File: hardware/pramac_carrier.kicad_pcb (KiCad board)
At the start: 2 copper layers, 135 x 100 mm, 31 parts, among them J1 BATT+ / BATT-, J2 TAHO / CONTACT / GND, J3 Relay module VCC/IN1/IN2/GND, P1 LM2596 IN+/IN-, P2 LM2596 OUT+/OUT-, U1A ESP32 left, U1B ESP32 right, U3 LM393

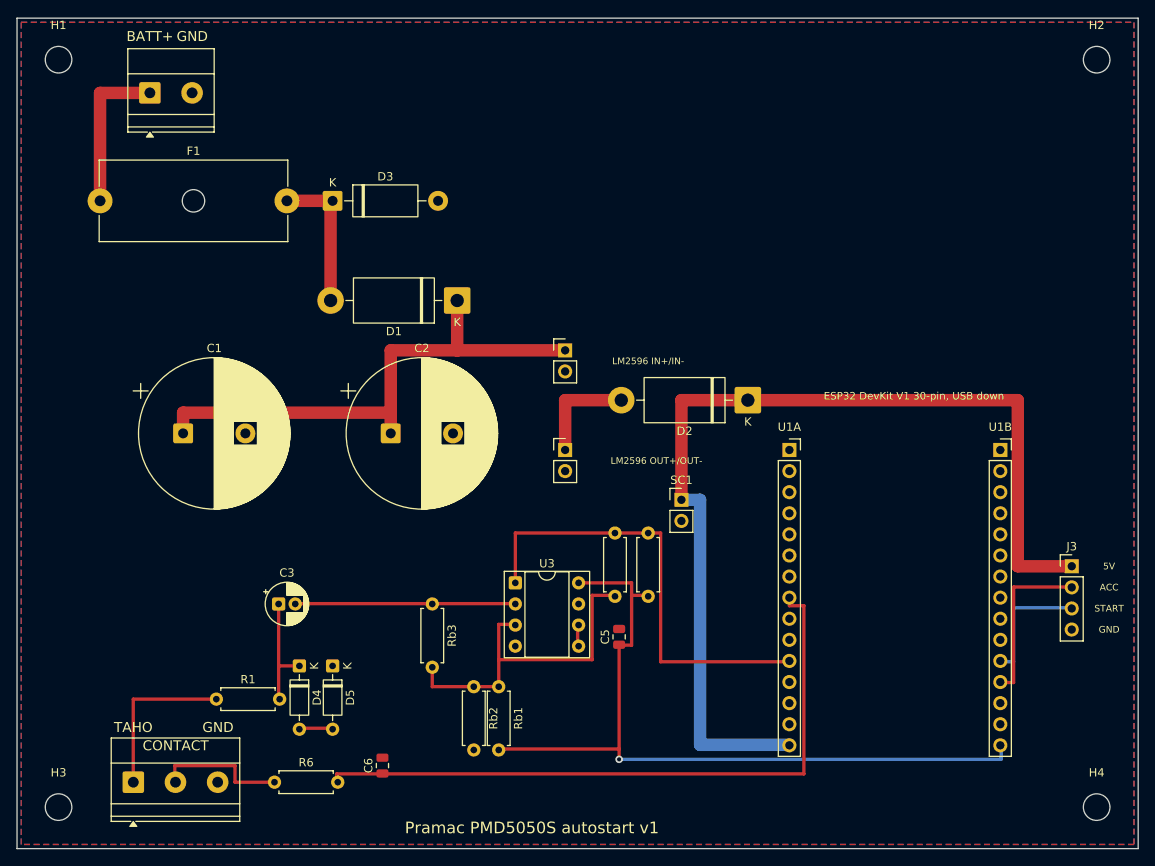
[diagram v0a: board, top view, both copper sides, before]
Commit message: Board v3: on-board relays with NPN drivers, RM20S DC-DC, charger input, one-side terminals, full BOM
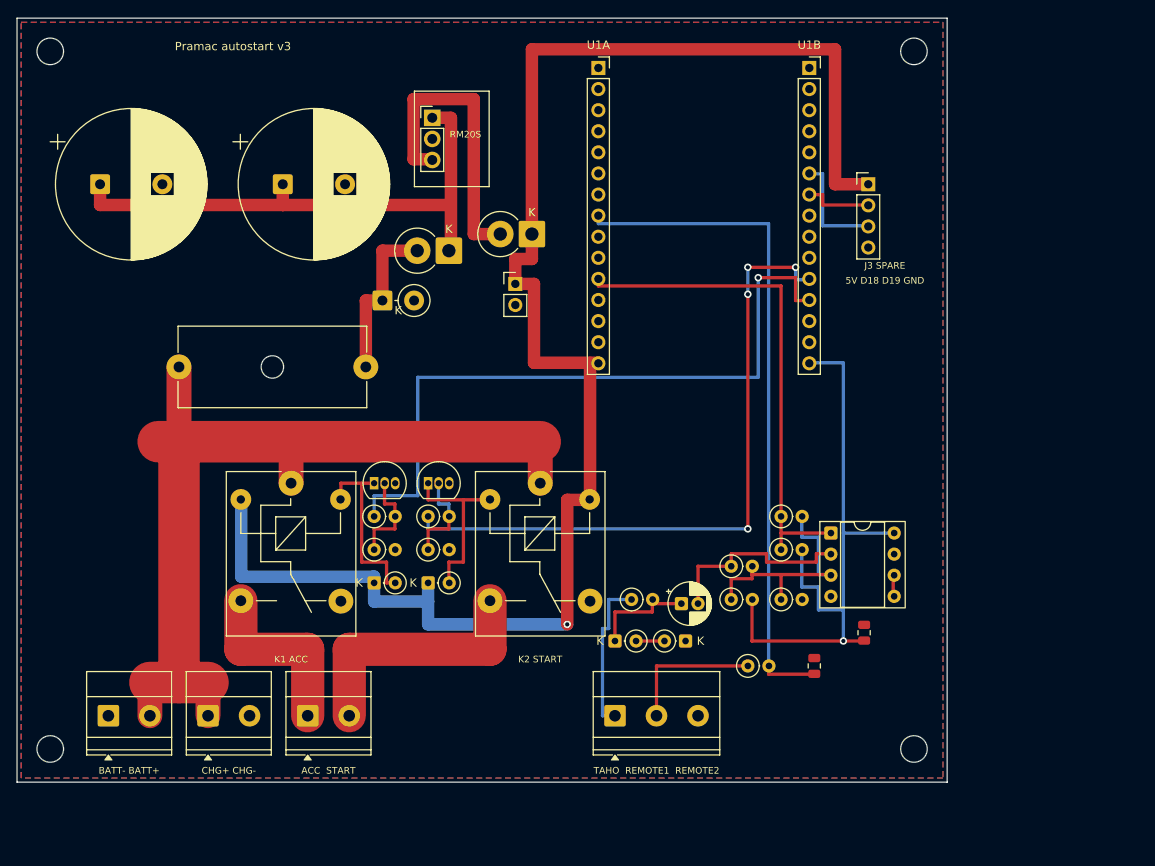
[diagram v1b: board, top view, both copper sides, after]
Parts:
- removed P1: LM2596 IN+/IN-, PinHeader_1x02_P2.54mm_Vertical
- removed P2: LM2596 OUT+/OUT-, PinHeader_1x02_P2.54mm_Vertical
- added D6: 1N4148, D_DO-35_SOD27_P2.54mm_Vertical_CathodeUp, F.Cu at (43.0, 68.0)
- added D7: 1N4148, D_DO-35_SOD27_P2.54mm_Vertical_CathodeUp, F.Cu at (49.5, 68.0)
- added J4: CHARGER +12V / GND, TerminalBlock_Phoenix_MKDS-1,5-2_1x02_P5.00mm_Horizontal, F.Cu at (23.0, 84.0)
- added J5: ACC OUT / START OUT (relay NO), TerminalBlock_Phoenix_MKDS-1,5-2_1x02_P5.00mm_Horizontal, F.Cu at (35.0, 84.0)
- added K1: SRD-05VDC-SL-C ACC, Relay_SPDT_SANYOU_SRD_Series_Form_C, F.Cu at (33.0, 56.0)
- added K2: SRD-05VDC-SL-C START, Relay_SPDT_SANYOU_SRD_Series_Form_C, F.Cu at (63.0, 56.0)
- added Q1: BC337, TO-92_Inline, F.Cu at (43.0, 56.0)
- added Q2: BC337, TO-92_Inline, F.Cu at (49.5, 56.0)
- added RM1: Favotek RM20S-050 SIP-3: 1 +VIN, 2 GND, 3 +VOUT, PinHeader_1x03_P2.54mm_Vertical, F.Cu at (50.0, 12.0)
- added Rp1: 10k, R_Axial_DIN0207_L6.3mm_D2.5mm_P2.54mm_Vertical, F.Cu at (43.0, 64.0)
- added Rp2: 10k, R_Axial_DIN0207_L6.3mm_D2.5mm_P2.54mm_Vertical, F.Cu at (49.5, 64.0)
- added Rv1: 10k, R_Axial_DIN0207_L6.3mm_D2.5mm_P2.54mm_Vertical, F.Cu at (86.0, 70.0)
- added Rv2: 10k, R_Axial_DIN0207_L6.3mm_D2.5mm_P2.54mm_Vertical, F.Cu at (92.0, 70.0)
- D1, D2: footprint D_DO-201AD_P15.24mm_Horizontal -> D_DO-201AD_P3.81mm_Vertical_CathodeUp
- D3: value P6KE36A -> P6KE36A (P6KE20A recommended); footprint D_DO-15_P12.70mm_Horizontal -> D_DO-15_P3.81mm_Vertical_CathodeUp
- D4, D5: footprint D_DO-35_SOD27_P7.62mm_Horizontal -> D_DO-35_SOD27_P2.54mm_Vertical_CathodeUp
- F1: value Fuse 5x20 -> Fuse 5x20 T2A
- J1: value BATT+ / BATT- -> BATT- / BATT+; footprint TerminalBlock_Phoenix_MKDS-1,5-2-5.08_1x02_P5.08mm_Horizontal -> TerminalBlock_Phoenix_MKDS-1,5-2_1x02_P5.00mm_Horizontal
- J2: value TAHO / CONTACT / GND -> TAHO / REMOTE 1 / REMOTE 2; footprint TerminalBlock_Phoenix_MKDS-1,5-3-5.08_1x03_P5.08mm_Horizontal -> TerminalBlock_Phoenix_MKDS-1,5-3_1x03_P5.00mm_Horizontal
- J3: value Relay module VCC/IN1/IN2/GND -> Spare relay module 5V/IN1(D18)/IN2(D19)/GND
- R1, R4, R5, R6, Rb3: footprint R_Axial_DIN0207_L6.3mm_D2.5mm_P7.62mm_Horizontal -> R_Axial_DIN0207_L6.3mm_D2.5mm_P2.54mm_Vertical
- Rb1, Rb2: value 10k -> 1k; footprint R_Axial_DIN0207_L6.3mm_D2.5mm_P7.62mm_Horizontal -> R_Axial_DIN0207_L6.3mm_D2.5mm_P2.54mm_Vertical
- moved J1 75.2 mm to (11.0, 84.0)
- moved R6 58.7 mm to (88.0, 78.0)
- moved J2 58.5 mm to (72.0, 84.0)
- moved C6 53.4 mm to (96.0, 78.0)
- moved J3 52.1 mm to (102.5, 20.0)
- moved U1A 51.4 mm to (70.0, 6.00)
- moved U1B 51.4 mm to (95.4, 6.00)
- moved R1 51.4 mm to (74.0, 70.0)
- moved C3 48.5 mm to (80.0, 70.5)
- moved D5 42.6 mm to (80.5, 75.0), turned to 180 degrees
- moved U3 38.5 mm to (98.0, 62.0)
- moved D4 38.1 mm to (72.0, 75.0), turned to 0 degrees
- moved Rb3 36.3 mm to (86.0, 66.0), turned to 0 degrees
- moved D2 32.8 mm to (62.0, 26.0)
- moved SC1 32.8 mm to (60.0, 32.0)
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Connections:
- J1 pad 1: VBATT -> GND
- J1 pad 2: GND -> VBATT
- J3 pad 2: ACC -> EXT1
- J3 pad 3: START -> EXT2
- Rb1 pad 1: VB -> ACC
- Rb1 pad 2: 3V3 -> BASE_ACC
- Rb2 pad 1: VB -> START
- Rb2 pad 2: GND -> BASE_START
- U1B pad 6: (no net) -> EXT2
- U1B pad 7: (no net) -> EXT1
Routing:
- net VBATT: track 19.0 -> 109.0 mm
- net NODE_B: track 121.6 -> 197.5 mm, vias 0 -> 1
- net START: track 15.1 -> 80.5 mm, vias 0 -> 4
- net ACC: track 20.0 -> 84.0 mm, vias 0 -> 1
- net START_OUT: track 0.00 -> 30.8 mm
- net VBUCK: track 12.8 -> 36.3 mm
- net COIL_ACC: track 0.00 -> 22.0 mm
- net ACC_OUT: track 0.00 -> 21.9 mm
- net COIL_START: track 0.00 -> 21.3 mm
- net 3V3: track 93.9 -> 74.5 mm
- net EXT2: track 0.00 -> 13.3 mm
- net VB: track 41.7 -> 29.6 mm
- net BASE_START: track 0.00 -> 11.8 mm
- net BASE_ACC: track 0.00 -> 11.8 mm
- net EXT1: track 0.00 -> 8.29 mm
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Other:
- board size 135 x 100 mm -> 112 x 92 mm
- board text added: "5V D18 D19 GND"
- board text added: "ACC START"
- board text added: "BATT- BATT+"
- board text added: "CHG+ CHG-"
- board text added: "J3 SPARE"
- board text added: "K1 ACC"
- board text added: "K2 START"
- board text added: "Pramac autostart v3"
- board text added: "RM20S"
- board text added: "TAHO REMOTE1 REMOTE2"
- board text removed: "5V"
- board text removed: "ACC"
- board text removed: "BATT+"
- board text removed: "CONTACT"
- board text removed: "ESP32 DevKit V1 30-pin, USB down"
- board text removed: "GND"
- board text removed: "LM2596 IN+/IN-"
- board text removed: "LM2596 OUT+/OUT-"
- board text removed: "Pramac PMD5050S autostart v1"
- board text removed: "START"
- board text removed: "TAHO"

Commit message: Board v4: contactor relay K3, radial fuse, per-pin silk labels, QR/GitHub mark on back; firmware: contactor warm-up/cool-down logic
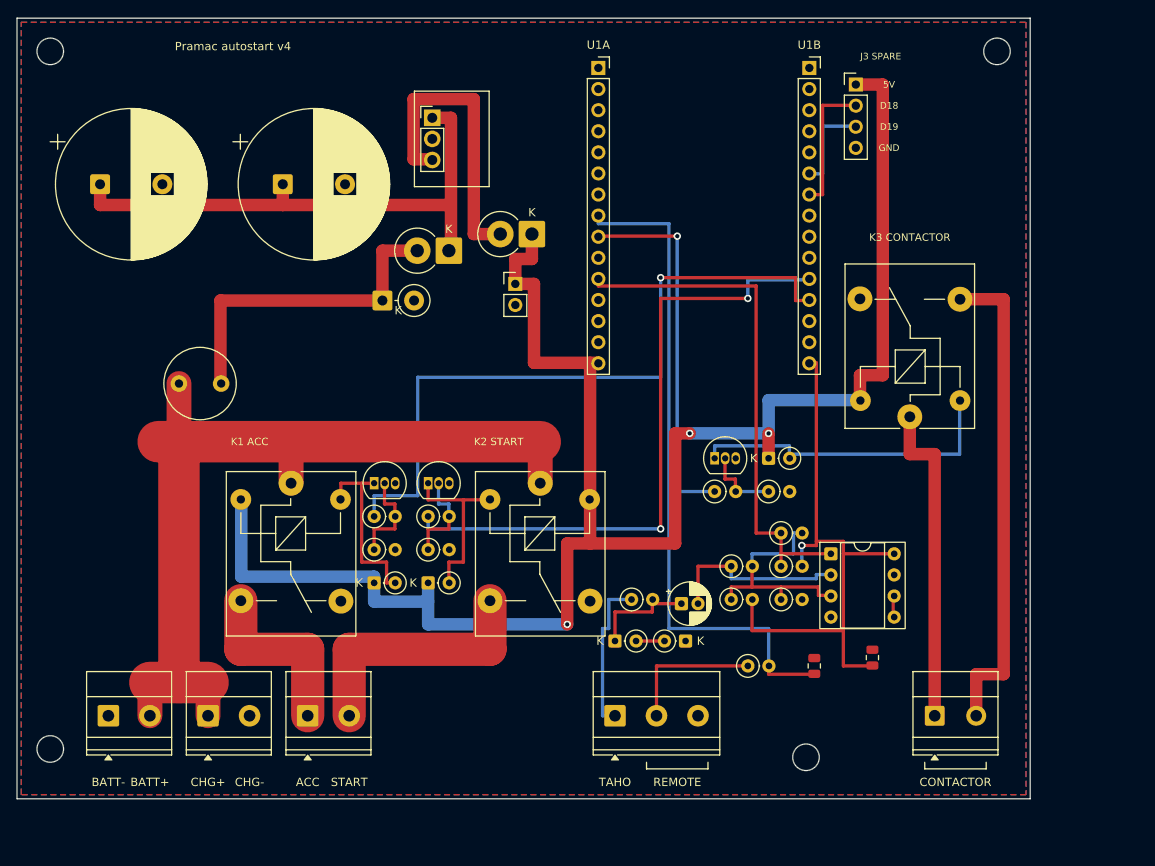
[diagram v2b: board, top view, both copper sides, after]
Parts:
- added D8: 1N4148, D_DO-35_SOD27_P2.54mm_Vertical_CathodeUp, F.Cu at (90.5, 53.0)
- added J6: CONTACTOR (relay K3 dry COM/NO, 230V), TerminalBlock_Phoenix_MKDS-1,5-2_1x02_P5.00mm_Horizontal, F.Cu at (110.5, 84.0)
- added K3: SRD-05VDC-SL-A CONTACTOR, Relay_SPDT_SANYOU_SRD_Series_Form_C, F.Cu at (107.5, 48.0)
- added Q3: BC337, TO-92_Inline, F.Cu at (84.0, 53.0)
- added Rg3: 1k, R_Axial_DIN0207_L6.3mm_D2.5mm_P2.54mm_Vertical, F.Cu at (84.0, 57.0)
- added Rp3: 10k, R_Axial_DIN0207_L6.3mm_D2.5mm_P2.54mm_Vertical, F.Cu at (90.5, 57.0)
- F1: value Fuse 5x20 T2A -> KLS5-102-5RT-020H 2A slow; footprint Fuseholder_Cylinder-5x20mm_Schurter_0031_8201_Horizontal_Open -> Fuse_Littelfuse_372_D8.50mm
- J2: value TAHO / REMOTE 1 / REMOTE 2 -> TAHO / REMOTE
- moved H4 13.0 mm to (95.0, 89.0)
- moved J3 12.1 mm to (101.0, 8.00)
- moved H2 10.0 mm to (118.0, 4.00)
- moved C5 3.16 mm to (103.0, 77.0)
- moved U3 2.50 mm to (98.0, 64.5)
- moved F1 2.00 mm to (19.5, 44.0)
- moved R4 2.00 mm to (92.0, 62.0)
- moved R5 2.00 mm to (92.0, 66.0)
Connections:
- U1A pad 9: (no net) -> CONT
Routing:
- net CT_NO: track 0.00 -> 58.7 mm
- net CONT: track 0.00 -> 44.8 mm, vias 0 -> 1
- net COIL_CONT: track 0.00 -> 39.0 mm
- net CT_COM: track 0.00 -> 39.0 mm
- net VBF: track 20.3 -> 39.8 mm
- net NODE_B: track 197.5 -> 215.3 mm, vias 1 -> 3
- net BASE_CONT: track 0.00 -> 9.27 mm
- net EXT1: track 8.29 -> 16.3 mm
- net 3V3: track 74.5 -> 69.8 mm
- net START: track 80.5 -> 77.5 mm, vias 4 -> 2
- net VBATT: track 109.0 -> 107.0 mm
- net CMP_OUT: track 60.6 -> 62.6 mm
- net EXT2: track 13.3 -> 11.3 mm
- net TAHO_AC: track 24.0 -> 22.5 mm
- net VB: track 29.6 -> 28.6 mm
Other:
- board size 112 x 92 mm -> 122 x 94 mm
- board text added: "4106677"
- board text added: "5V"
- board text added: "ACC"
- board text added: "BATT+"
- board text added: "BATT-"
- board text added: "CHG+"
- board text added: "CHG-"
- board text added: "CONTACTOR"
- board text added: "D18"
- board text added: "D19"
- board text added: "GND"
- board text added: "K3 CONTACTOR"
- board text added: "Pramac autostart v4"
- board text added: "REMOTE"
- board text added: "START"
- board text added: "TAHO"
- board text added: "github.com/4106677"
- board text added: "pramac-pmd5050s-autostart"
- board text removed: "5V D18 D19 GND"
- board text removed: "ACC START"
- board text removed: "BATT- BATT+"
- board text removed: "CHG+ CHG-"
- board text removed: "Pramac autostart v3"
- board text removed: "RM20S"
- board text removed: "TAHO REMOTE1 REMOTE2"

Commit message: Board v4: shift VBATT/relay assembly left, board 118x94 mm
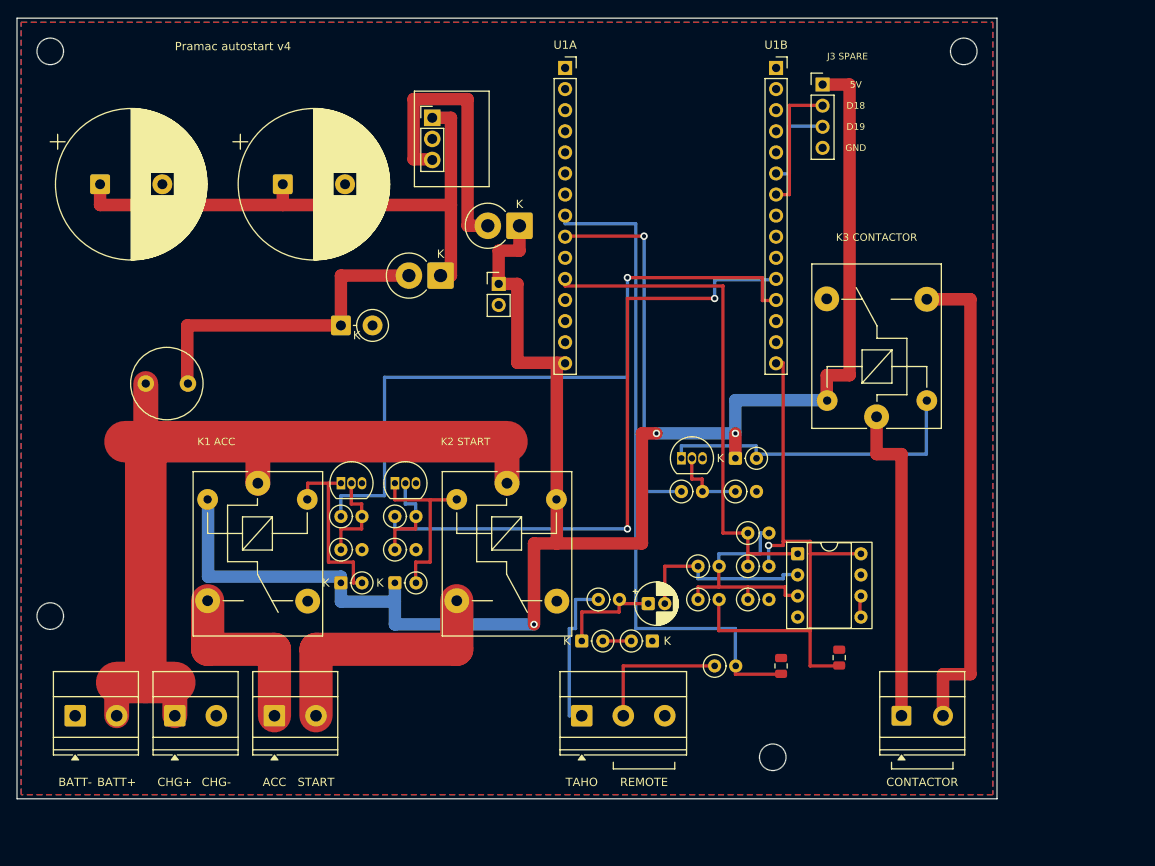
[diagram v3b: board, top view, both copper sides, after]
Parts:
- moved H3 16.0 mm to (4.00, 72.0)
- moved D3 5.83 mm to (39.0, 37.0)
- moved C3 4.00 mm to (76.0, 70.5)
- moved C5 4.00 mm to (99.0, 77.0)
- moved C6 4.00 mm to (92.0, 78.0)
- moved D4 4.00 mm to (68.0, 75.0)
- moved D5 4.00 mm to (76.5, 75.0)
- moved D6 4.00 mm to (39.0, 68.0)
- moved D7 4.00 mm to (45.5, 68.0)
- moved D8 4.00 mm to (86.5, 53.0)
- moved F1 4.00 mm to (15.5, 44.0)
- moved H2 4.00 mm to (114.0, 4.00)
- moved H4 4.00 mm to (91.0, 89.0)
- moved J1 4.00 mm to (7.00, 84.0)
- moved J2 4.00 mm to (68.0, 84.0)
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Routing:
- net NODE_A: track 65.8 -> 69.8 mm
- net VBUCK: track 36.3 -> 33.8 mm
- net NODE_B: track 215.3 -> 214.8 mm
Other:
- board size 122 x 94 mm -> 118 x 94 mm

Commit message: Board v5: minimal size 93.2x82 mm (horizontal ESP32, parts under module, antenna keep-out)
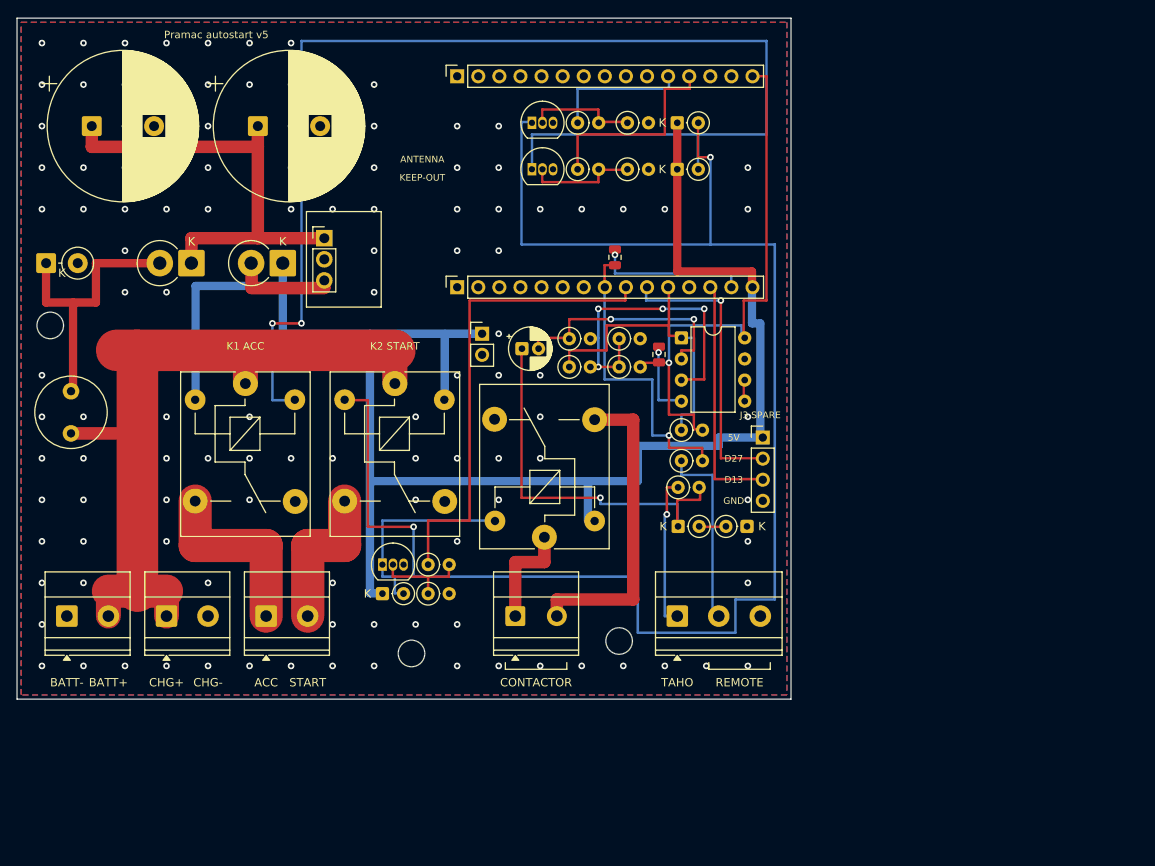
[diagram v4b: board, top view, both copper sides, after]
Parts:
- removed H4: M3, MountingHole_3.2mm_M3
- J3: value Spare relay module 5V/IN1(D18)/IN2(D19)/GND -> Spare relay module 5V/IN1(D27)/IN2(D13)/GND
- K1: value SRD-05VDC-SL-C ACC -> SRD-05VDC-SL-A ACC
- K2: value SRD-05VDC-SL-C START -> SRD-05VDC-SL-A START
- U1A: value ESP32 left -> ESP32 bottom row
- U1B: value ESP32 right -> ESP32 top row
- U3: value LM393 -> LM393 (soldered, no socket); footprint DIP-8_W7.62mm_Socket -> DIP-8_W7.62mm
- moved H2 98.4 mm to (47.5, 76.5)
- moved H3 68.6 mm to (72.5, 75.0)
- moved D7 65.0 mm to (79.5, 12.6)
- moved D6 64.2 mm to (79.5, 18.2)
- moved Rp2 58.5 mm to (73.5, 12.6)
- moved Rp1 57.3 mm to (73.5, 18.2)
- moved C6 53.1 mm to (72.0, 28.8)
- moved Rb2 52.3 mm to (67.5, 12.6)
- moved Rb1 50.6 mm to (67.5, 18.2)
- moved J6 48.0 mm to (60.0, 72.0)
- moved Q2 46.4 mm to (62.0, 12.6)
- moved D8 45.5 mm to (44.0, 69.3)
- moved Q1 44.2 mm to (62.0, 18.2)
- moved J3 43.1 mm to (89.8, 50.5)
- moved K3 42.5 mm to (63.5, 62.5)
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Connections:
- K3 pad 2: COIL_CONT -> NODE_B
- K3 pad 5: NODE_B -> COIL_CONT
- U1A pad 10: (no net) -> EXT1
- U1A pad 13: (no net) -> EXT2
- U1B pad 14: GND -> (no net)
- U1B pad 6: EXT2 -> (no net)
- U1B pad 7: EXT1 -> (no net)
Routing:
- net COIL_START: track 21.3 -> 189.5 mm, vias 0 -> 2
- net COIL_ACC: track 22.0 -> 153.6 mm, vias 0 -> 2
- net START: track 77.5 -> 16.6 mm, vias 2 -> 0
- net ACC: track 84.0 -> 24.8 mm, vias 1 -> 0
- net D25: track 81.3 -> 36.6 mm, vias 0 -> 1
- net TAHO_CL: track 13.0 -> 47.9 mm, vias 0 -> 1
- net GND: track 0.00 -> 28.2 mm, vias 0 -> 120
- net CT_COM: track 39.0 -> 13.0 mm
- net CMP_OUT: track 62.6 -> 38.7 mm
- net CT_NO: track 58.7 -> 37.5 mm
- net VBUCK: track 33.8 -> 12.8 mm
- net EXT1: track 16.3 -> 34.6 mm, vias 0 -> 1
- net EXT2: track 11.3 -> 29.3 mm
- net NODE_A: track 69.8 -> 55.0 mm
- net COIL_CONT: track 39.0 -> 24.9 mm
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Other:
- board size 118 x 94 mm -> 93.2 x 82 mm
- board text added: "ANTENNA"
- board text added: "D13"
- board text added: "D27"
- board text added: "KEEP-OUT"
- board text added: "Pramac autostart v5"
- board text removed: "D18"
- board text removed: "D19"
- board text removed: "K3 CONTACTOR"
- board text removed: "Pramac autostart v4"
- board text removed: "github.com/4106677"
- board text removed: "pramac-pmd5050s-autostart"
